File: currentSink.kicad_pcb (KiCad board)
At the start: 2 copper layers, 36 x 28 mm, 42 parts, among them P101 ExtBatt_Power, P102 uPower, P103 uSignals, P104 Load+ve, P105 Load-ve, P106 PowerSwitch, P202 TST, P302 TST, Q201 BUK9575, U201 LMV358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

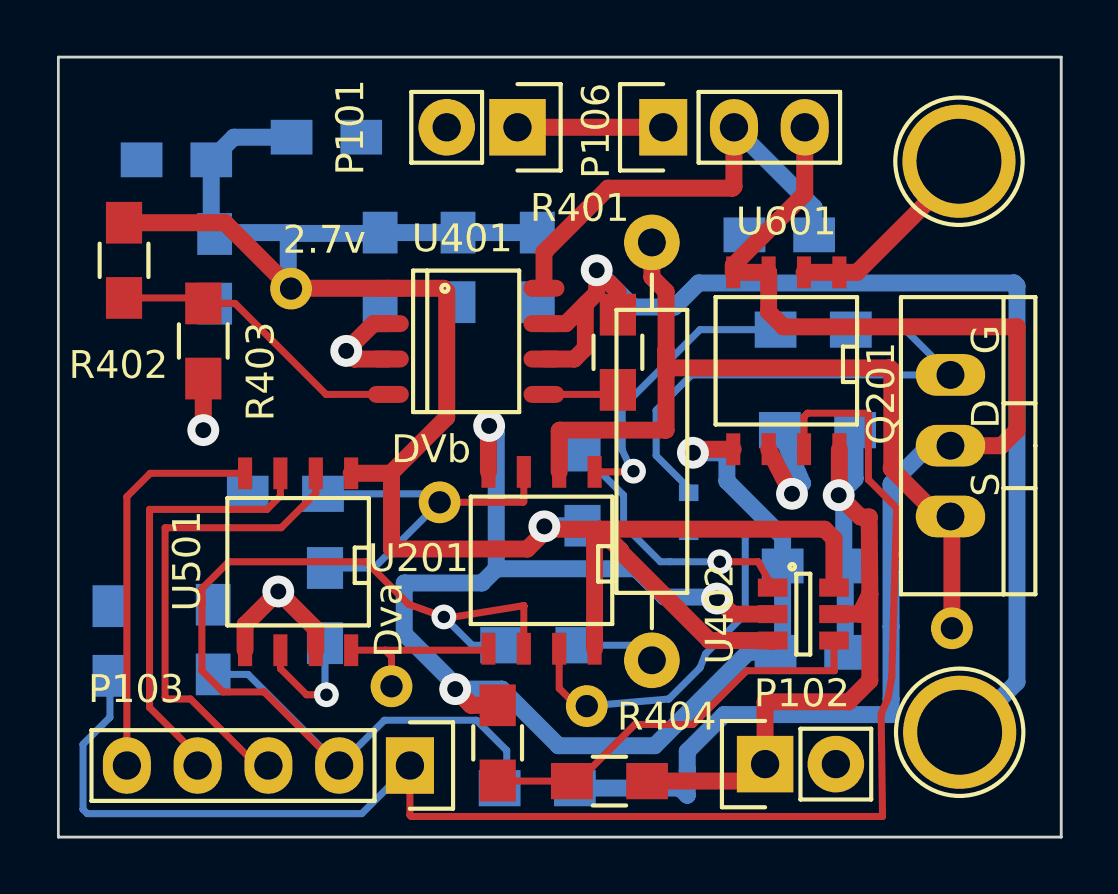
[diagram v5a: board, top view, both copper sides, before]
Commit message: reduced board six to 34mm
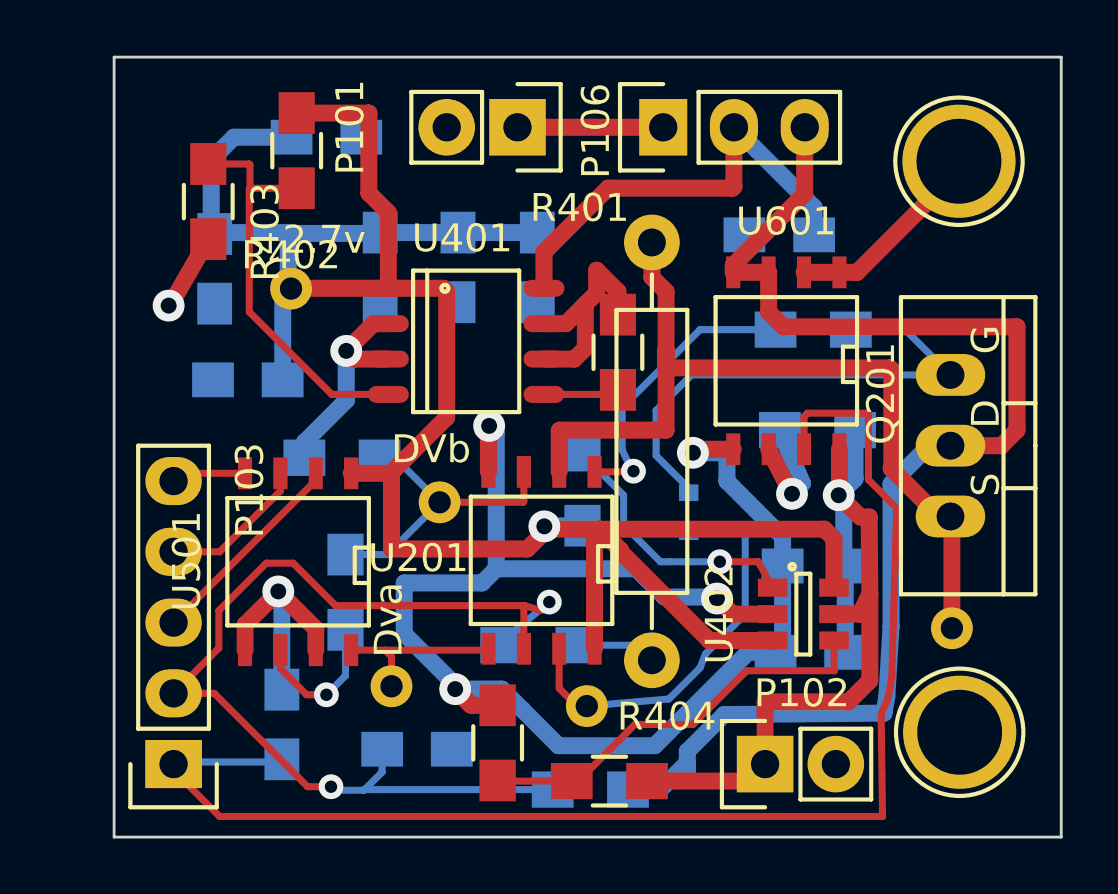
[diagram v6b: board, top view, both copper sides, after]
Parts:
- moved P103 8.48 mm to (145.1, 119.4), turned to 180 degrees
- moved C302 8.31 mm to (153.9, 118.8), turned to 0 degrees
- moved C501 8.31 mm to (147.8, 105.6)
- moved R402 7.34 mm to (149.6, 97.4)
- moved C601 6.86 mm to (149.0, 118.0)
- moved R403 5.01 mm to (146.4, 99.2)
- moved R204 2.41 mm to (151.2, 108.4)
- moved R301 1.91 mm to (160.1, 120.3)
- moved R203 0.88 mm to (151.3, 113.2)
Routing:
- net GND: track 106.1 -> 80.7 mm, vias 8 -> 7
- net /Micro Control/SDI: track 14.2 -> 2.68 mm
- net /Micro Control/SCK: track 15.6 -> 5.38 mm
- net /Micro Control/~CS: track 17.5 -> 7.47 mm
- net /Current Read/Current_Read: track 55.0 -> 48.1 mm
- net 2.7V: track 75.5 -> 81.1 mm
- net Net-(R402-Pad2): track 10.9 -> 14.7 mm
- net /Voltage Control/VoltageRead: track 40.9 -> 37.7 mm, vias 1 -> 2
- net /Current Read/CurrentSink_Out: track 49.2 -> 46.4 mm
- net Net-(P201-Pad1): track 13.5 -> 11.1 mm
- net /Current Control/DAC_Vb: track 4.57 -> 5.32 mm
- removed copper zone on B.Cu, net GND
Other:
- board size 36 x 28 mm -> 34 x 28 mm

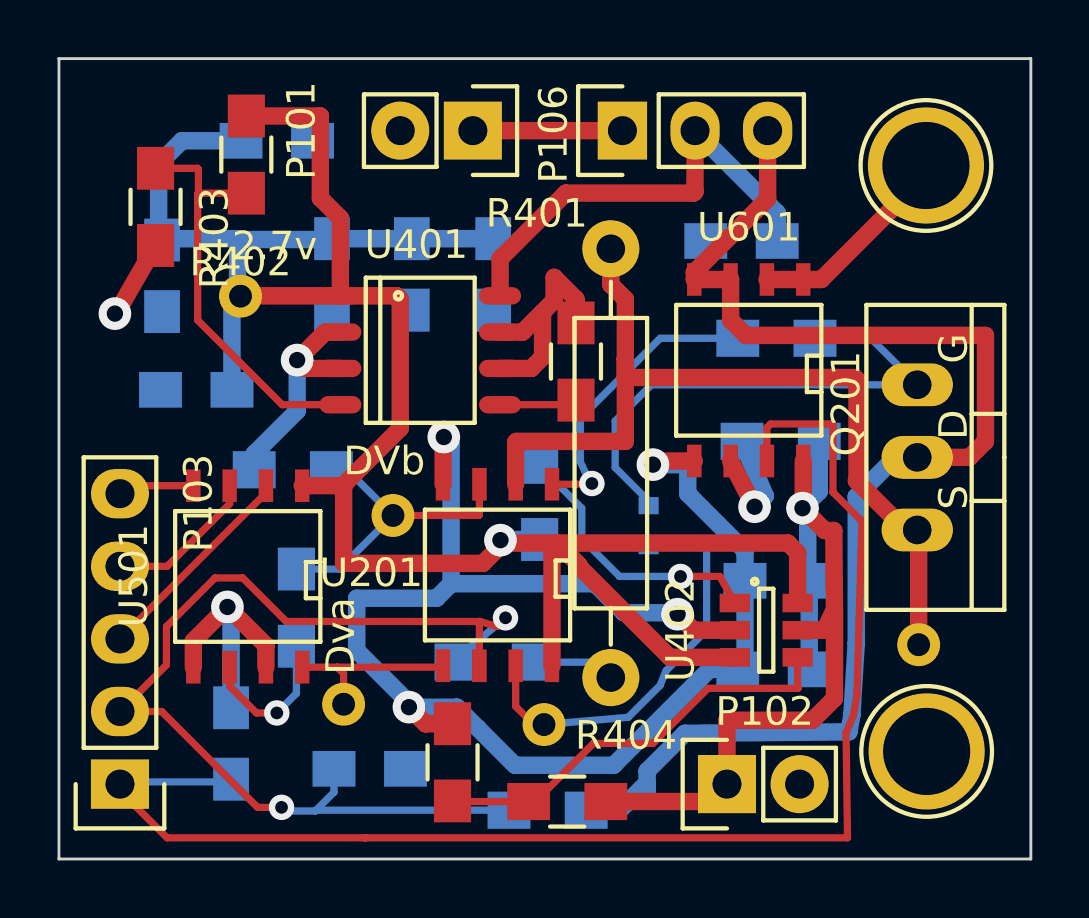
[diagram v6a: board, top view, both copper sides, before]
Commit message: adjusted board sixe to 34mm x 28mm
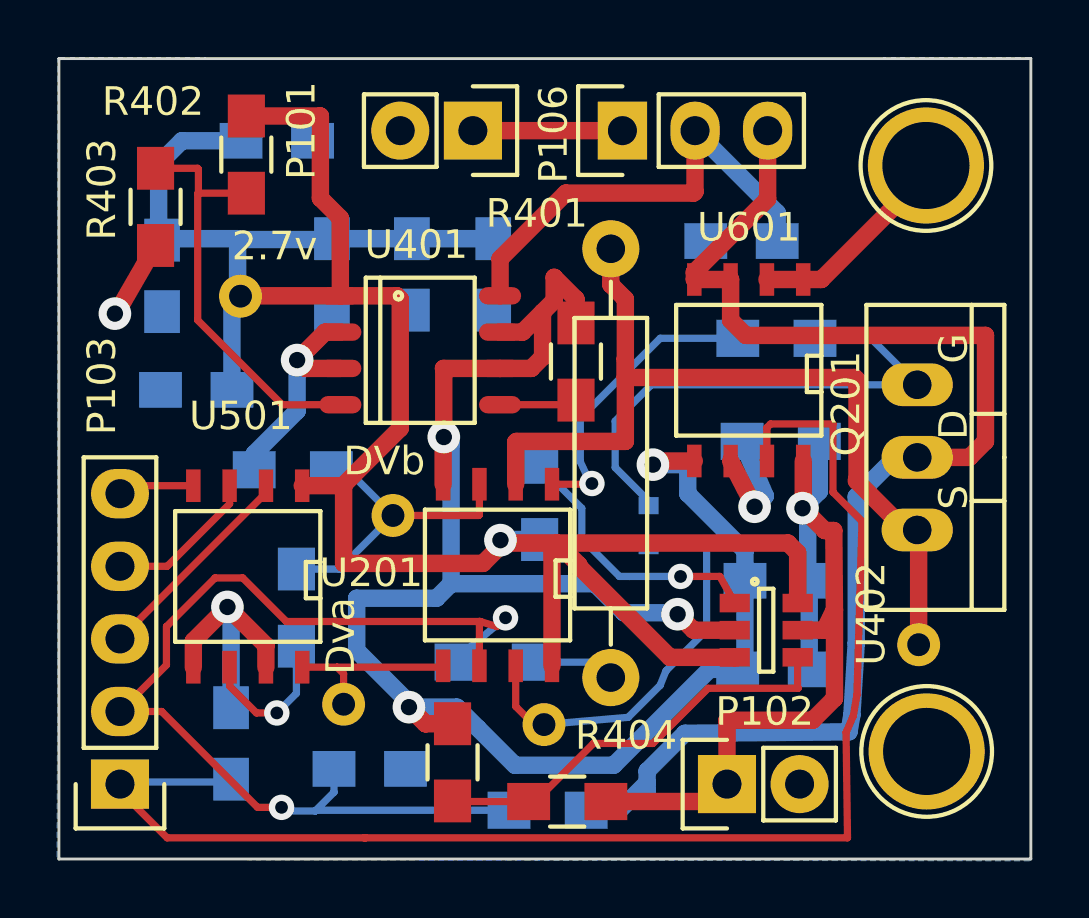
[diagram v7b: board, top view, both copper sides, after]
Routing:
- net GND: track 80.7 -> 85.1 mm
- added copper zone on B.Cu, net GND

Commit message: added gerber files that have been submitted
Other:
- rule trace_min: 0.2 -> 0.1524
- rule via_min_drill: 0.3 -> 0.3048
- rule via_min_size: 0.4 -> 0.508
- board text added: "CSOS v0.1"
